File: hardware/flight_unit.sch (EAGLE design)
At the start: 31 parts, among them IC2 7805T, J1 CONN_20X2SHROUDED, T1 THERMISTOR-2,5, U1 4MB Flash, U2 4MB Flash, U3 4MB Flash, X1 S4B-ZR, X2 S4B-ZR

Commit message: working on routing...
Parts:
- added R2: 1k, resistor:R-US_R1210
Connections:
- new net HOLD_PUP2: R2.1
- net +3V3: now also R2.2
- net LED_0: now also U$1.7/RX2; no longer U$1.5
- net LED_2: now also U$1.5; no longer U$1.7/RX2
- net SC_D0: now also U$1.2; no longer U$1.0/RX1
- net SC_D2: now also U$1.0/RX1; no longer U$1.2
- net T_0: now also U$1.17/A3/TX4; no longer U$1.14/A0/TX3
- net V_0: now also U$1.14/A0/TX3; no longer U$1.16/A2/RX4
- net V_1: now also U$1.16/A2/RX4; no longer U$1.17/A3/TX4
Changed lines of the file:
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@@
 <part name="H2" library="SparkFun-Retired" deviceset="SEW_HOLE" device=""/>
 <part name="GND15" library="SparkFun-PowerSymbols" library_urn="urn:adsk.eagle:library:530" deviceset="GND" device=""/>
+<part name="R2" library="resistor" library_urn="urn:adsk.eagle:library:348" deviceset="R-US_" device="R1210" package3d_urn="urn:adsk.eagle:package:23554/2" value="1k"/>
+<part name="+3V12" library="supply1" deviceset="+3V3" device=""/>
 </parts>
 <sheets>
@@
 </segment>
 </net>
-<net name="SC_D0" class="0">
+<net name="SC_D1" class="0">
+<segment>
+<pinref part="U$1" gate="G$1" pin="1/TX1"/>
+<wire x1="114.3" y1="106.68" x2="99.06" y2="106.68" width="0.1524" layer="91"/>
+<label x="91.44" y="106.68" size="1.778" layer="95"/>
+</segment>
+</net>
+<net name="SC_D2" class="0">
 <segment>
 <pinref part="U$1" gate="G$1" pin="0/RX1"/>
@@
 </segment>
 </net>
-<net name="SC_D1" class="0">
-<segment>
-<pinref part="U$1" gate="G$1" pin="1/TX1"/>
-<wire x1="114.3" y1="106.68" x2="99.06" y2="106.68" width="0.1524" layer="91"/>
-<label x="91.44" y="106.68" size="1.778" layer="95"/>
-</segment>
-</net>
-<net name="SC_D2" class="0">
+<net name="SC_D3" class="0">
+<segment>
+<pinref part="U$1" gate="G$1" pin="3"/>
+<wire x1="114.3" y1="101.6" x2="99.06" y2="101.6" width="0.1524" layer="91"/>
+<label x="91.44" y="101.6" size="1.778" layer="95"/>
+</segment>
+</net>
+<net name="SC_D4" class="0">
+<segment>
+<pinref part="U$1" gate="G$1" pin="4"/>
+<wire x1="114.3" y1="99.06" x2="99.06" y2="99.06" width="0.1524" layer="91"/>
+<label x="91.44" y="99.06" size="1.778" layer="95"/>
+</segment>
+</net>
+<net name="LED_0" class="0">
+<segment>
+<pinref part="U$1" gate="G$1" pin="7/RX2"/>
+<wire x1="114.3" y1="91.44" x2="99.06" y2="91.44" width="0.1524" layer="91"/>
+<label x="91.44" y="91.44" size="1.778" layer="95"/>
+</segment>
+</net>
+<net name="LED_1" class="0">
+<segment>
+<pinref part="U$1" gate="G$1" pin="6"/>
+<wire x1="114.3" y1="93.98" x2="99.06" y2="93.98" width="0.1524" layer="91"/>
+<label x="91.44" y="93.98" size="1.778" layer="95"/>
+</segment>
+</net>
+<net name="T_1" class="0">
+<segment>
+<pinref part="U$1" gate="G$1" pin="15/A1/RX3"/>
+<wire x1="154.94" y1="83.82" x2="170.18" y2="83.82" width="0.1524" layer="91"/>
+<label x="170.18" y="83.82" size="1.778" layer="95"/>
+</segment>
+</net>
+<net name="V_0" class="0">
+<segment>
+<pinref part="U$1" gate="G$1" pin="14/A0/TX3"/>
+<wire x1="154.94" y1="81.28" x2="170.18" y2="81.28" width="0.1524" layer="91"/>
+<label x="170.18" y="81.28" size="1.778" layer="95"/>
+</segment>
+</net>
+<net name="V_1" class="0">
+<segment>
+<pinref part="U$1" gate="G$1" pin="16/A2/RX4"/>
+<wire x1="154.94" y1="86.36" x2="170.18" y2="86.36" width="0.1524" layer="91"/>
+<label x="170.18" y="86.36" size="1.778" layer="95"/>
+</segment>
+</net>
+<net name="A_0" class="0">
+<segment>
+<pinref part="U$1" gate="G$1" pin="20/A6/TX5"/>
+<wire x1="154.94" y1="96.52" x2="170.18" y2="96.52" width="0.1524" layer="91"/>
+<label x="170.18" y="96.52" size="1.778" layer="95"/>
+</segment>
+</net>
+<net name="A_1" class="0">
+<segment>
+<pinref part="U$1" gate="G$1" pin="21/A7/RX5"/>
+<wire x1="154.94" y1="99.06" x2="170.18" y2="99.06" width="0.1524" layer="91"/>
+<label x="170.18" y="99.06" size="1.778" layer="95"/>
+</segment>
+</net>
+<net name="A_2" class="0">
+<segment>
+<pinref part="U$1" gate="G$1" pin="22/A8"/>
+<wire x1="154.94" y1="101.6" x2="170.18" y2="101.6" width="0.1524" layer="91"/>
+<label x="170.18" y="101.6" size="1.778" layer="95"/>
+</segment>
+</net>
+<net name="A_3" class="0">
+<segment>
+<pinref part="U$1" gate="G$1" pin="23/A9"/>
+<wire x1="154.94" y1="104.14" x2="170.18" y2="104.14" width="0.1524" layer="91"/>
+<label x="170.18" y="104.14" size="1.778" layer="95"/>
+</segment>
+</net>
+<net name="NC" class="0">
+<segment>
+<pinref part="U$1" gate="G$1" pin="3V3_LO"/>
+<wire x1="154.94" y1="106.68" x2="170.18" y2="106.68" width="0.1524" layer="91"/>
+<label x="170.18" y="106.68" size="1.778" layer="95"/>
+</segment>
+</net>
+<net name="MEM_CS2" class="0">
+<segment>
+<pinref part="U$1" gate="G$1" pin="10/CS"/>
+<wire x1="114.3" y1="83.82" x2="99.06" y2="83.82" width="0.1524" layer="91"/>
+<label x="86.36" y="83.82" size="1.778" layer="95"/>
+</segment>
+</net>
+<net name="LED_2" class="0">
+<segment>
+<pinref part="U$1" gate="G$1" pin="5"/>
+<wire x1="114.3" y1="96.52" x2="99.06" y2="96.52" width="0.1524" layer="91"/>
+<label x="91.44" y="96.52" size="1.778" layer="95"/>
+</segment>
+</net>
+<net name="SC_D0" class="0">
 <segment>
 <pinref part="U$1" gate="G$1" pin="2"/>
@@
 </segment>
 </net>
-<net name="SC_D3" class="0">
-<segment>
-<pinref part="U$1" gate="G$1" pin="3"/>
-<wire x1="114.3" y1="101.6" x2="99.06" y2="101.6" width="0.1524" layer="91"/>
-<label x="91.44" y="101.6" size="1.778" layer="95"/>
-</segment>
-</net>
-<net name="SC_D4" class="0">
-<segment>
-<pinref part="U$1" gate="G$1" pin="4"/>
-<wire x1="114.3" y1="99.06" x2="99.06" y2="99.06" width="0.1524" layer="91"/>
-<label x="91.44" y="99.06" size="1.778" layer="95"/>
-</segment>
-</net>
-<net name="LED_0" class="0">
-<segment>
-<pinref part="U$1" gate="G$1" pin="5"/>
-<wire x1="114.3" y1="96.52" x2="99.06" y2="96.52" width="0.1524" layer="91"/>
-<label x="91.44" y="96.52" size="1.778" layer="95"/>
-</segment>
-</net>
-<net name="LED_1" class="0">
-<segment>
-<pinref part="U$1" gate="G$1" pin="6"/>
-<wire x1="114.3" y1="93.98" x2="99.06" y2="93.98" width="0.1524" layer="91"/>
-<label x="91.44" y="93.98" size="1.778" layer="95"/>
-</segment>
-</net>
-<net name="LED_2" class="0">
-<segment>
-<pinref part="U$1" gate="G$1" pin="7/RX2"/>
-<wire x1="114.3" y1="91.44" x2="99.06" y2="91.44" width="0.1524" layer="91"/>
-<label x="91.44" y="91.44" size="1.778" layer="95"/>
-</segment>
-</net>
 <net name="T_0" class="0">
-<segment>
-<pinref part="U$1" gate="G$1" pin="14/A0/TX3"/>
-<wire x1="154.94" y1="81.28" x2="170.18" y2="81.28" width="0.1524" layer="91"/>
-<label x="170.18" y="81.28" size="1.778" layer="95"/>
-</segment>
-</net>
-<net name="T_1" class="0">
-<segment>
-<pinref part="U$1" gate="G$1" pin="15/A1/RX3"/>
-<wire x1="154.94" y1="83.82" x2="170.18" y2="83.82" width="0.1524" layer="91"/>
-<label x="170.18" y="83.82" size="1.778" layer="95"/>
-</segment>
-</net>
-<net name="V_0" class="0">
-<segment>
-<pinref part="U$1" gate="G$1" pin="16/A2/RX4"/>
-<wire x1="154.94" y1="86.36" x2="170.18" y2="86.36" width="0.1524" layer="91"/>
-<label x="170.18" y="86.36" size="1.778" layer="95"/>
-</segment>
-</net>
-<net name="V_1" class="0">
 <segment>
 <pinref part="U$1" gate="G$1" pin="17/A3/TX4"/>
 <wire x1="154.94" y1="88.9" x2="170.18" y2="88.9" width="0.1524" layer="91"/>
 <label x="170.18" y="88.9" size="1.778" layer="95"/>
-</segment>
-</net>
-<net name="A_0" class="0">
-<segment>
-<pinref part="U$1" gate="G$1" pin="20/A6/TX5"/>
-<wire x1="154.94" y1="96.52" x2="170.18" y2="96.52" width="0.1524" layer="91"/>
-<label x="170.18" y="96.52" size="1.778" layer="95"/>
-</segment>
-</net>
-<net name="A_1" class="0">
-<segment>
-<pinref part="U$1" gate="G$1" pin="21/A7/RX5"/>
-<wire x1="154.94" y1="99.06" x2="170.18" y2="99.06" width="0.1524" layer="91"/>
-<label x="170.18" y="99.06" size="1.778" layer="95"/>
-</segment>
-</net>
-<net name="A_2" class="0">
-<segment>
-<pinref part="U$1" gate="G$1" pin="22/A8"/>
-<wire x1="154.94" y1="101.6" x2="170.18" y2="101.6" width="0.1524" layer="91"/>
-<label x="170.18" y="101.6" size="1.778" layer="95"/>
-</segment>
-</net>
-<net name="A_3" class="0">
-<segment>
-<pinref part="U$1" gate="G$1" pin="23/A9"/>
-<wire x1="154.94" y1="104.14" x2="170.18" y2="104.14" width="0.1524" layer="91"/>
-<label x="170.18" y="104.14" size="1.778" layer="95"/>
-</segment>
-</net>
-<net name="NC" class="0">
-<segment>
-<pinref part="U$1" gate="G$1" pin="3V3_LO"/>
-<wire x1="154.94" y1="106.68" x2="170.18" y2="106.68" width="0.1524" layer="91"/>
-<label x="170.18" y="106.68" size="1.778" layer="95"/>
-</segment>
-</net>
-<net name="MEM_CS2" class="0">
-<segment>
-<pinref part="U$1" gate="G$1" pin="10/CS"/>
-<wire x1="114.3" y1="83.82" x2="99.06" y2="83.82" width="0.1524" layer="91"/>
-<label x="86.36" y="83.82" size="1.778" layer="95"/>
 </segment>
 </net>
@@
 <attribute name="VALUE" x="69.85" y="118.11" size="1.778" layer="96"/>
 </instance>
+<instance part="R2" gate="G$1" x="50.8" y="147.32" smashed="yes" rot="R90">
+<attribute name="NAME" x="56.9214" y="151.13" size="1.778" layer="95" rot="R180"/>
+<attribute name="VALUE" x="56.642" y="146.05" size="1.778" layer="96" rot="R180"/>
+</instance>
+<instance part="+3V12" gate="G$1" x="50.8" y="158.75" smashed="yes">
+<attribute name="VALUE" x="52.07" y="158.75" size="1.778" layer="96"/>
+</instance>
 </instances>
 <busses>
@@
 <wire x1="68.58" y1="109.22" x2="68.58" y2="115.57" width="0.1524" layer="91"/>
 </segment>
+<segment>
+<pinref part="+3V12" gate="G$1" pin="+3V3"/>
+<pinref part="R2" gate="G$1" pin="2"/>
+<wire x1="50.8" y1="156.21" x2="50.8" y2="152.4" width="0.1524" layer="91"/>
+</segment>
 </net>
 <net name="GND" class="0">
@@
 </segment>
 </net>
+<net name="HOLD_PUP2" class="0">
+<segment>
+<pinref part="R2" gate="G$1" pin="1"/>
+<wire x1="50.8" y1="142.24" x2="50.8" y2="137.16" width="0.1524" layer="91"/>
+<label x="45.72" y="134.62" size="1.778" layer="95"/>
+</segment>
+</net>

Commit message: few more tweaks.
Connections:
- net HOLD_PUP: no longer U1.!HOLD
- net HOLD_PUP2: now also U1.!HOLD
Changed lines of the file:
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@@
-</segment>
-<segment>
-<pinref part="U1" gate="G$1" pin="!HOLD"/>
-<wire x1="63.5" y1="106.68" x2="71.12" y2="106.68" width="0.1524" layer="91"/>
-<label x="71.12" y="106.68" size="1.778" layer="95"/>
 </segment>
 <segment>
@@
 <label x="45.72" y="134.62" size="1.778" layer="95"/>
 </segment>
+<segment>
+<pinref part="U1" gate="G$1" pin="!HOLD"/>
+<wire x1="63.5" y1="106.68" x2="71.12" y2="106.68" width="0.1524" layer="91"/>
+<label x="71.12" y="106.68" size="1.778" layer="95"/>
+</segment>
 </net>

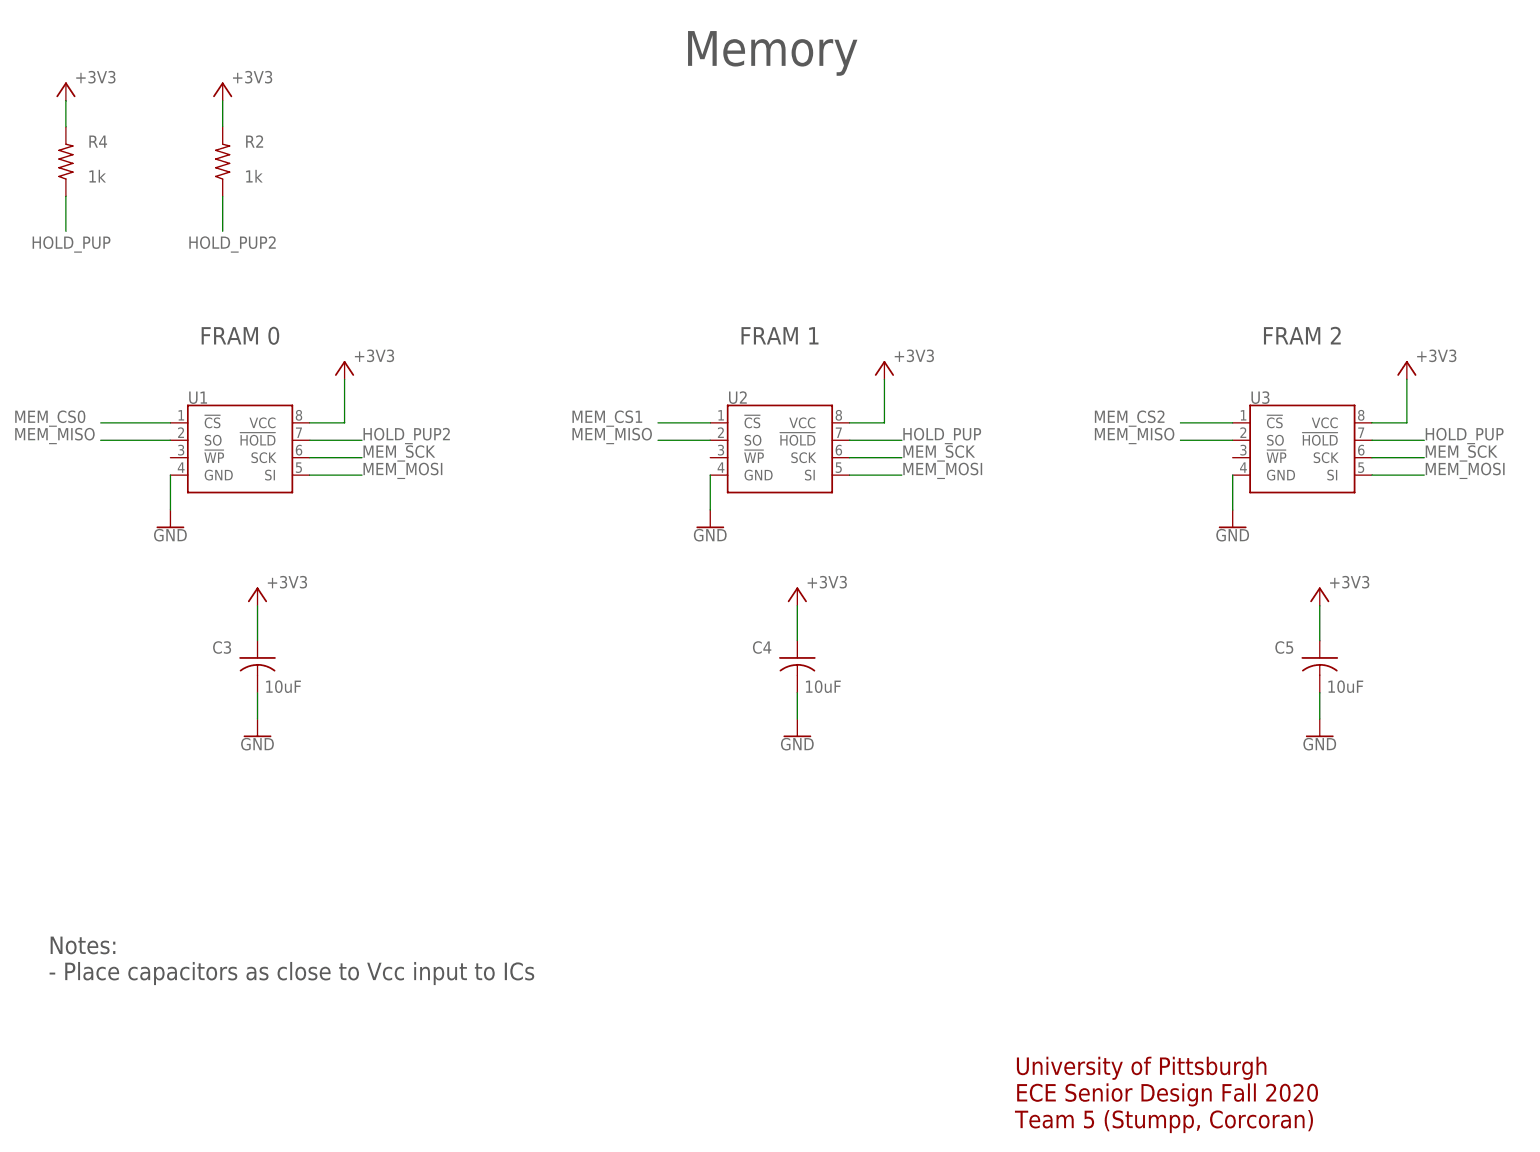
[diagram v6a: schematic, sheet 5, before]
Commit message: finalized preliminary routing
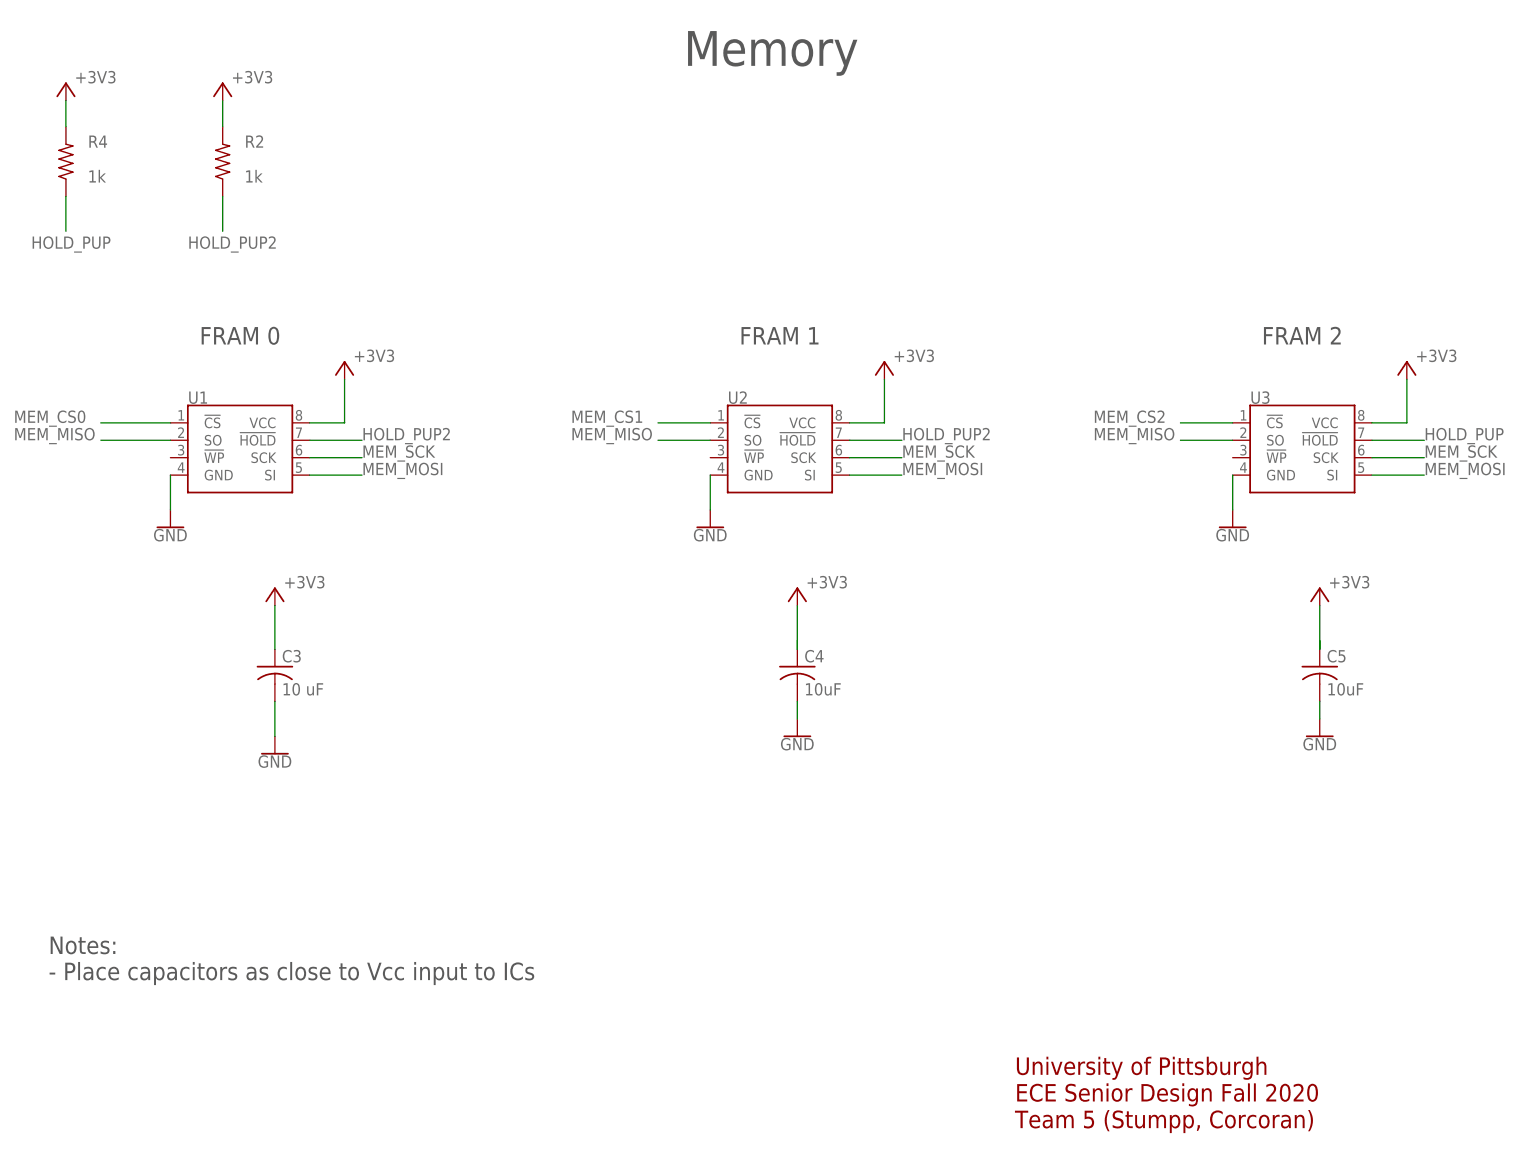
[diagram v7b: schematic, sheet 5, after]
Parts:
- C3: value 10uF -> 10 uF; device adafruit:C-US025-040X050 -> adafruit:C-USC0805K
- C4, C5: device adafruit:C-US025-040X050 -> adafruit:C-USC0805K
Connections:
- net HOLD_PUP: no longer U2.!HOLD
- net HOLD_PUP2: now also U2.!HOLD
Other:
- moved on the sheet: C3, C4, C5

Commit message: updates before purchase order
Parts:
- removed R1: 3.3k, rcl:R-US_0207/10
- removed X1, X2: S4B-ZR, con-jst:S4B-ZR
- added BATTERY, SUPPLY: (no value), adafruit:JST_2PIN-THM
- added R3: 1k, adafruit:R-US_R0805
- C1: value 0.1uf -> 1 uF; device capacitor-wima:C2,5-3 -> adafruit:C-USC0805K
- C2: value 0.1uf -> .1 uF; device capacitor-wima:C2,5-3 -> adafruit:C-USC0805K
- R2, R4, R5, R6: device resistor:R-US_R1210 -> adafruit:R-US_R0805
- R7: value 1k -> 2.2k; device resistor:R-US_R1210 -> adafruit:R-US_R0805
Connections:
- removed net N$13: LED2.A, R5.2
- new net N$3: LED2.A, R3.1
- net GND: now also BATTERY.1, SUPPLY.1; no longer X1-2.1, X2-2.1
- net HOLD_PUP: now also R2.1; no longer R4.1
- net HOLD_PUP2: now also R4.1; no longer R2.1
- net LED_0: now also R6.2; no longer R7.1
- net LED_1: now also R5.2; no longer R6.1
- net LED_2: now also R3.2; no longer R5.1
- net N$1: now also BATTERY.2, R7.1; no longer R1.1, X1-1.1
- net N$2: now also R7.2; no longer R1.2
- net N$4: now also SUPPLY.2; no longer X2-1.1
- net N$7: now also R6.1; no longer R7.2
- net N$8: now also R5.1; no longer R6.2
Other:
- note removed: "Backup Battery Input"
- note removed: "ISS Power Source"
- moved on the sheet: C1, C2, R2, R4, R5, R6
